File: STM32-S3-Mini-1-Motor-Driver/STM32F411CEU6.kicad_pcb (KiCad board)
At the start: 2 copper layers, 77.3 x 60.5 mm, 46 parts, among them J1 USB_C_Receptacle_USB2.0, J10 5V, J11 3.3V, J12 4.5-36V, J2 MOTOR_1_OUT, J3 MOTOR_2_OUT, J4 MOTOR_3_OUT, J5 MOTOR_4_OUT, J6 Conn_01x15_Pin, J7 Conn_01x12_Pin, J8 Conn_01x02_Pin, SW2 EN, SW3 SLW-66527511-SMT-TR, U1 PCAL6408ABS, U2 ESP32-S3-MINI-1, U3 PRTR5V0U2X, U4 L293D, U5 TPS62160DSG, U6 L293D

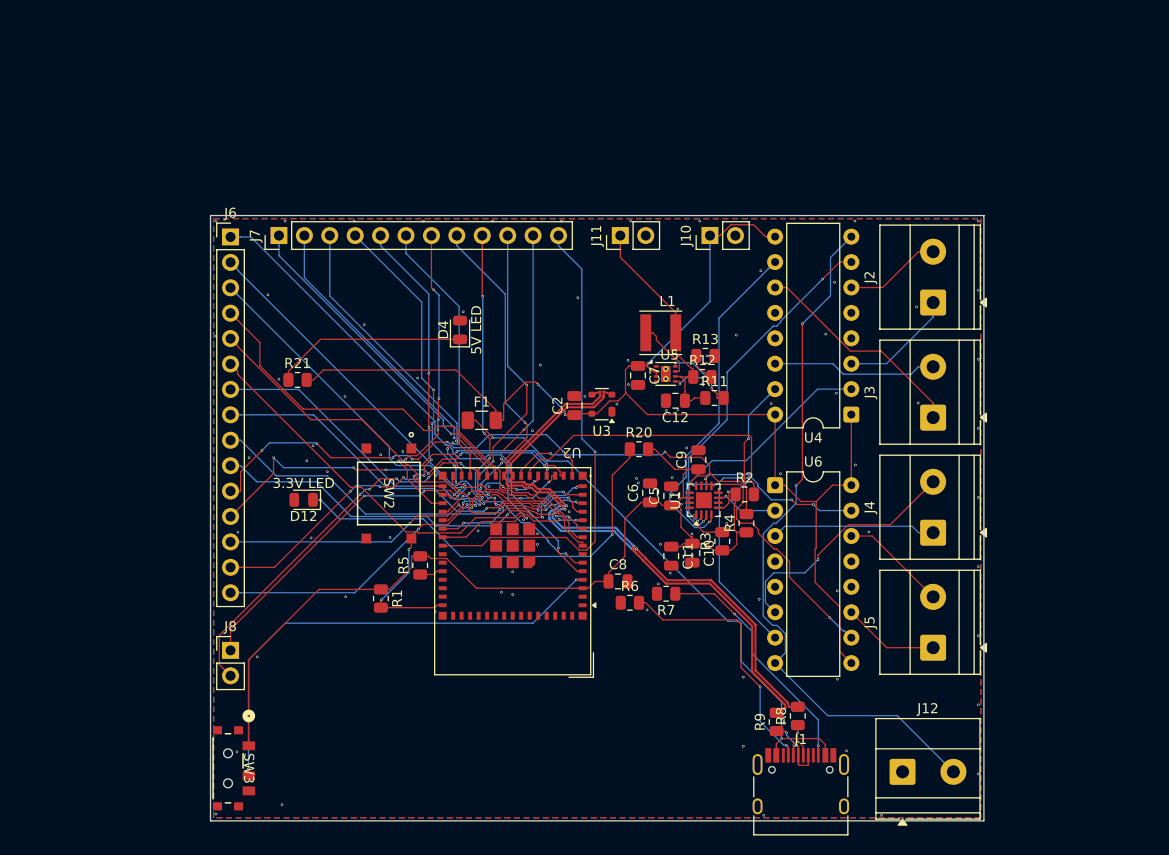
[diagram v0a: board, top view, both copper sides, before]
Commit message: Get reverse polarity detected
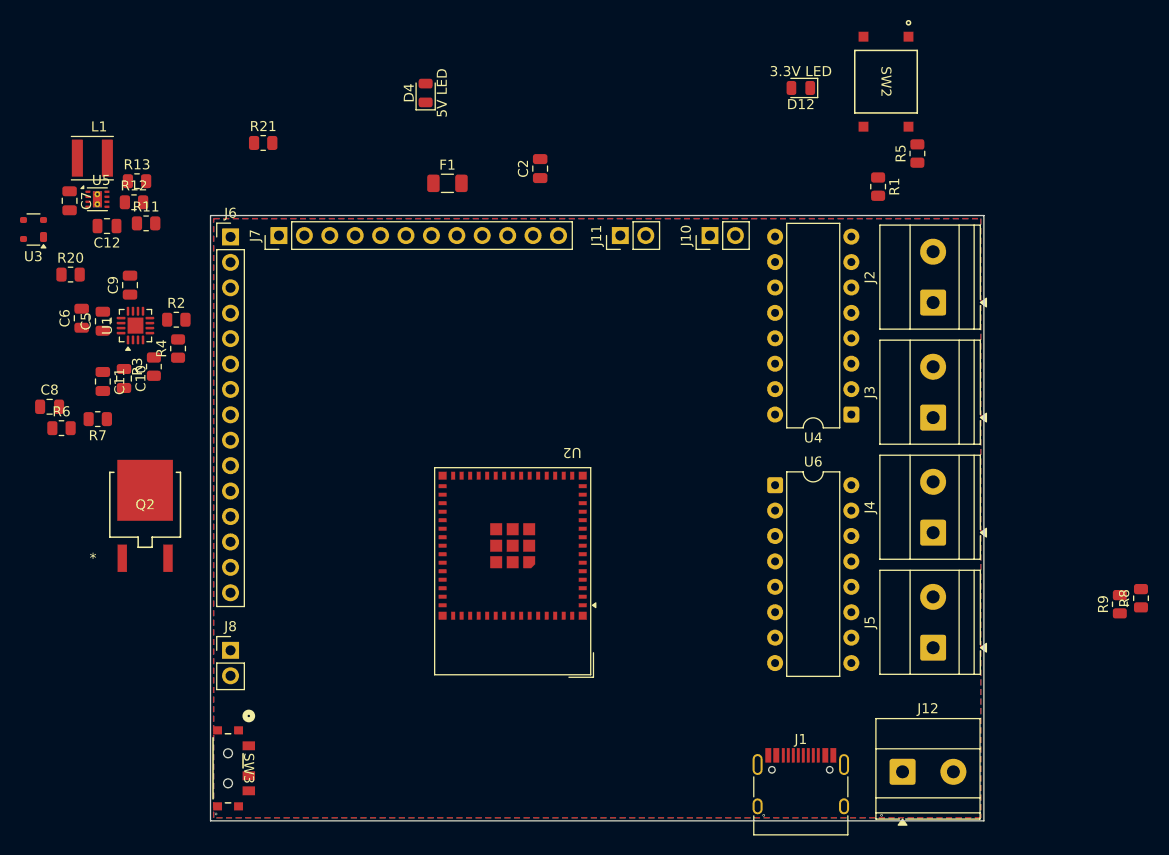
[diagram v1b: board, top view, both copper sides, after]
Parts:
- added Q2: AOD4185, ul_AOD4185:TO252_AOS, F.Cu at (158.2, 78.4)
- moved D12 64.5 mm to (223.8, 36.8)
- moved R5 64.5 mm to (235.4, 43.3)
- moved SW2 64.5 mm to (232.3, 36.1)
- moved R1 64.5 mm to (231.5, 46.6)
- moved C10 59.4 mm to (156.1, 65.8)
- moved C11 59.4 mm to (154.0, 66.1)
- moved C12 59.4 mm to (154.4, 50.6)
- moved C5 59.4 mm to (154.0, 60.1)
- moved C6 59.4 mm to (151.9, 59.8)
- moved C7 59.4 mm to (150.7, 48.0)
- moved C8 59.4 mm to (148.7, 68.6)
- moved C9 59.4 mm to (156.7, 56.5)
- moved R11 59.4 mm to (158.3, 50.3)
- moved R13 59.4 mm to (157.4, 46.1)
- moved R2 59.4 mm to (161.3, 59.9)
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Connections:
- J12 pad 2: /4.5-36V -> Net-(J12-Pin_2)
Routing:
- net +5V: track 126.0 -> 0.00 mm, vias 3 -> 0
- net +3V3: track 93.0 -> 0.00 mm
- net /4.5-36V: track 70.3 -> 0.00 mm, vias 2 -> 0
- net D-: track 60.3 -> 0.00 mm, vias 2 -> 0
- net D+: track 59.7 -> 0.00 mm, vias 2 -> 0
- net VBUS: track 56.5 -> 0.00 mm, vias 2 -> 0
- net Net-(J6-Pin_1): track 52.6 -> 0.00 mm, vias 1 -> 0
- net Net-(J7-Pin_12): track 48.6 -> 0.00 mm, vias 1 -> 0
- net Net-(J6-Pin_2): track 48.4 -> 0.00 mm, vias 1 -> 0
- net /BOOTMODE: track 48.3 -> 0.00 mm, vias 2 -> 0
- net Net-(J6-Pin_4): track 47.6 -> 0.00 mm
- net Net-(J6-Pin_3): track 47.4 -> 0.00 mm, vias 1 -> 0
- net Net-(J6-Pin_5): track 44.6 -> 0.00 mm, vias 2 -> 0
- net Net-(J6-Pin_6): track 43.6 -> 0.00 mm, vias 2 -> 0
- net Net-(D12-K): track 42.4 -> 0.00 mm, vias 2 -> 0
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
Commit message: Ues jlcpcb basic part where applicable
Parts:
- moved SW2 69.9 mm to (180.0, 82.6), turned to 0 degrees
- moved R6 66.7 mm to (216.5, 72.7), turned to 90 degrees
- moved R7 64.0 mm to (217.4, 66.7), turned to -90 degrees
- moved L1 61.9 mm to (209.8, 68.4), turned to -90 degrees
- moved R1 61.5 mm to (178.2, 77.2)
- moved C12 61.0 mm to (210.3, 74.9), turned to 0 degrees
- moved C7 60.5 mm to (205.7, 73.3)
- moved R5 60.4 mm to (184.5, 75.7)
- moved R12 60.2 mm to (212.1, 72.6)
- moved U5 60.2 mm to (208.4, 72.3)
- moved R11 60.1 mm to (212.1, 77.1)
- moved R13 59.7 mm to (208.5, 77.1), turned to 180 degrees
- moved C8 56.4 mm to (204.2, 78.7), turned to 90 degrees
- moved Q2 50.5 mm to (208.4, 84.3), turned to 90 degrees
- moved R3 50.5 mm to (209.4, 59.9), turned to 180 degrees
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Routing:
- net +5V: track 0.00 -> 126.1 mm
- net +3V3: track 0.00 -> 102.2 mm, vias 0 -> 4
- net VBUS: track 0.00 -> 74.6 mm, vias 0 -> 2
- net D-: track 0.00 -> 73.5 mm, vias 0 -> 2
- net D+: track 0.00 -> 71.3 mm
- net Net-(J6-Pin_1): track 0.00 -> 56.1 mm
- net Net-(J7-Pin_12): track 0.00 -> 52.8 mm, vias 0 -> 1
- net /4.5-36V: track 0.00 -> 52.4 mm, vias 0 -> 1
- net /BOOTMODE: track 0.00 -> 48.8 mm
- net Net-(J6-Pin_2): track 0.00 -> 48.8 mm, vias 0 -> 1
- net Net-(J7-Pin_11): track 0.00 -> 46.6 mm, vias 0 -> 5
- net Net-(J6-Pin_3): track 0.00 -> 46.4 mm, vias 0 -> 1
- net Net-(J7-Pin_10): track 0.00 -> 46.1 mm, vias 0 -> 5
- net Net-(J6-Pin_4): track 0.00 -> 45.1 mm, vias 0 -> 1
- net Net-(J6-Pin_5): track 0.00 -> 43.6 mm, vias 0 -> 1
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
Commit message: You slongoid
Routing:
- net Net-(J6-Pin_14): track 37.3 -> 54.4 mm, vias 5 -> 1
- net Net-(J6-Pin_12): track 36.0 -> 52.7 mm, vias 3 -> 1
- net +3.3V: track 34.0 -> 47.1 mm, vias 3 -> 0
- net Net-(J7-Pin_7): track 33.4 -> 45.8 mm, vias 4 -> 1
- net Net-(J6-Pin_13): track 36.3 -> 47.4 mm, vias 5 -> 2
- net Net-(J6-Pin_10): track 37.3 -> 48.2 mm, vias 4 -> 1
- net +5V: track 126.1 -> 136.8 mm
- net Net-(J7-Pin_9): track 34.3 -> 44.4 mm, vias 7 -> 1
- net Net-(D4-K): track 15.3 -> 24.8 mm
- net /I2C1_SDA: track 25.8 -> 34.7 mm, vias 4 -> 2
- net Net-(U5-FB): track 9.23 -> 17.6 mm, vias 3 -> 4
- net Net-(J6-Pin_9): track 39.1 -> 47.4 mm, vias 3 -> 1
- net Net-(J6-Pin_11): track 38.2 -> 46.4 mm, vias 3 -> 2
- net Net-(J7-Pin_11): track 46.6 -> 54.5 mm, vias 5 -> 1
- net Net-(J6-Pin_8): track 39.2 -> 46.6 mm, vias 2 -> 1
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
